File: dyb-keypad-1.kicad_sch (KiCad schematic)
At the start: 11 parts, among them J1 Conn_01x10, SW1 SW_Push_LED, SW2 SW_SPDT

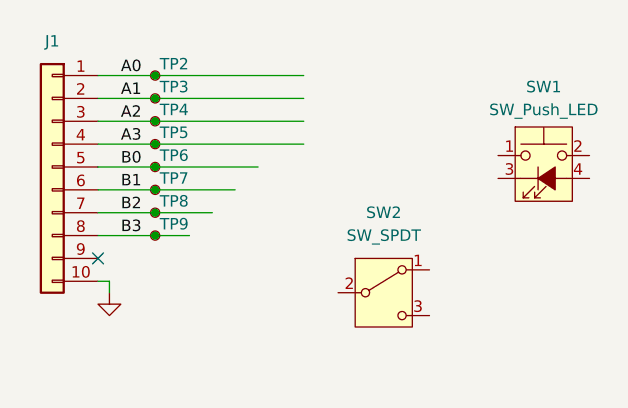
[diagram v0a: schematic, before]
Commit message: schem: fix output pin ordering
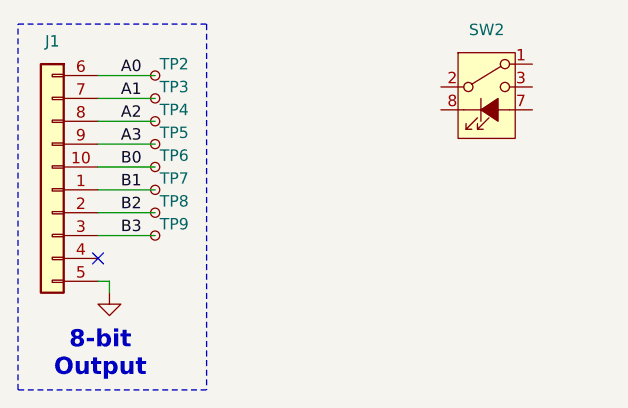
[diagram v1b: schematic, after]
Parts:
- removed SW1: SW_Push_LED, Button_Switch_THT:SW_NKK_GW12LJP, symbol Switch:SW_Push_LED
- removed SW2: SW_SPDT, Button_Switch_SMD:Nidec_Copal_CAS-120A, symbol Switch:SW_SPDT
- added SW2: SW_Push_LED_K6-6133D04, GLCS:SW_LED_K6-6133d04, symbol GLCS:SW_Push_LED_K6-6133D04
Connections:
- net A0: now also J1.6 (Pin_6); no longer J1.1 (Pin_1)
- net A1: now also J1.7 (Pin_7); no longer J1.2 (Pin_2)
- net A2: now also J1.8 (Pin_8); no longer J1.3 (Pin_3)
- net A3: now also J1.9 (Pin_9); no longer J1.4 (Pin_4)
- net B0: now also J1.10 (Pin_10); no longer J1.5 (Pin_5)
- net B1: now also J1.1 (Pin_1); no longer J1.6 (Pin_6)
- net B2: now also J1.2 (Pin_2); no longer J1.7 (Pin_7)
- net B3: now also J1.3 (Pin_3); no longer J1.8 (Pin_8)
- net GND: now also J1.5 (Pin_5); no longer J1.10 (Pin_10)
- new net: SW2.1, SW2.4
- new net: SW2.2, SW2.5
- new net: SW2.3, SW2.6
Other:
- note added: "8-bit Output"
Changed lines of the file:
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@@
 	(generator_version "10.0")
 	(paper "A4")
-	(junction
-		(at 58.42 62.23)
-		(diameter 0)
-		(color 0 0 0 0)
-	)
-	(junction
-		(at 58.42 44.45)
-		(diameter 0)
-		(color 0 0 0 0)
-	)
-	(junction
-		(at 58.42 46.99)
-		(diameter 0)
-		(color 0 0 0 0)
-	)
-	(junction
-		(at 58.42 59.69)
-		(diameter 0)
-		(color 0 0 0 0)
-	)
-	(junction
-		(at 58.42 57.15)
-		(diameter 0)
-		(color 0 0 0 0)
-	)
-	(junction
-		(at 58.42 52.07)
-		(diameter 0)
-		(color 0 0 0 0)
-	)
-	(junction
-		(at 58.42 54.61)
-		(diameter 0)
-		(color 0 0 0 0)
-	)
-	(junction
-		(at 58.42 49.53)
-		(diameter 0)
-		(color 0 0 0 0)
+	(rectangle
+		(start 43.18 38.735)
+		(end 64.135 79.375)
+		(stroke
+			(width 0)
+			(type dash)
+		)
+		(fill
+			(type none)
+		)
+	)
+	(text "8-bit\nOutput"
+		(exclude_from_sim no)
+		(at 52.324 75.438 0)
+		(effects
+			(font
+				(size 1.905 1.905)
+				(thickness 0.508)
+				(bold yes)
+			)
+		)
 	)
 	(no_connect
@@
 	(wire
 		(pts
-			(xy 58.42 62.23) (xy 62.23 62.23)
+			(xy 52.07 52.07) (xy 58.42 52.07)
 		)
 		(stroke
@@
 	(wire
 		(pts
-			(xy 52.07 52.07) (xy 58.42 52.07)
+			(xy 52.07 59.69) (xy 58.42 59.69)
 		)
 		(stroke
@@
 	(wire
 		(pts
-			(xy 52.07 59.69) (xy 58.42 59.69)
+			(xy 52.07 49.53) (xy 58.42 49.53)
 		)
 		(stroke
@@
 	(wire
 		(pts
-			(xy 52.07 49.53) (xy 58.42 49.53)
+			(xy 52.07 46.99) (xy 58.42 46.99)
 		)
 		(stroke
@@
 	(wire
 		(pts
-			(xy 58.42 59.69) (xy 64.77 59.69)
+			(xy 52.07 44.45) (xy 58.42 44.45)
 		)
 		(stroke
@@
 	(wire
 		(pts
-			(xy 52.07 46.99) (xy 58.42 46.99)
+			(xy 53.34 67.31) (xy 53.34 68.58)
 		)
 		(stroke
@@
 	(wire
 		(pts
-			(xy 58.42 57.15) (xy 67.31 57.15)
-		)
-		(stroke
-			(width 0)
-			(type default)
-		)
-	)
-	(wire
-		(pts
-			(xy 58.42 46.99) (xy 74.93 46.99)
-		)
-		(stroke
-			(width 0)
-			(type default)
-		)
-	)
-	(wire
-		(pts
-			(xy 52.07 44.45) (xy 58.42 44.45)
-		)
-		(stroke
-			(width 0)
-			(type default)
-		)
-	)
-	(wire
-		(pts
-			(xy 58.42 49.53) (xy 74.93 49.53)
-		)
-		(stroke
-			(width 0)
-			(type default)
-		)
-	)
-	(wire
-		(pts
-			(xy 53.34 67.31) (xy 53.34 68.58)
-		)
-		(stroke
-			(width 0)
-			(type default)
-		)
-	)
-	(wire
-		(pts
-			(xy 58.42 54.61) (xy 69.85 54.61)
-		)
-		(stroke
-			(width 0)
-			(type default)
-		)
-	)
-	(wire
-		(pts
 			(xy 52.07 57.15) (xy 58.42 57.15)
-		)
-		(stroke
-			(width 0)
-			(type default)
-		)
-	)
-	(wire
-		(pts
-			(xy 58.42 52.07) (xy 74.93 52.07)
-		)
-		(stroke
-			(width 0)
-			(type default)
-		)
-	)
-	(wire
-		(pts
-			(xy 58.42 44.45) (xy 74.93 44.45)
 		)
 		(stroke
@@
 	)
 	(symbol
-		(lib_id "Switch:SW_SPDT")
-		(at 83.82 68.58 0)
+		(lib_id "GLCS:SW_Push_LED_K6-6133D04")
+		(at 95.25 48.26 0)
 		(unit 1)
 		(body_style 1)
@@
 		(in_pos_files yes)
 		(dnp no)
-		(fields_autoplaced yes)
 		(property "Reference" "SW2"
-			(at 83.82 59.69 0)
-			(show_name no)
-			(do_not_autoplace no)
-			(effects
-				(font
-					(size 1.27 1.27)
-				)
-			)
-		)
-		(property "Value" "SW_SPDT"
-			(at 83.82 62.23 0)
-			(show_name no)
-			(do_not_autoplace no)
-			(effects
-				(font
-					(size 1.27 1.27)
-				)
-			)
-		)
-		(property "Footprint" "Button_Switch_SMD:Nidec_Copal_CAS-120A"
-			(at 83.82 68.58 0)
-			(hide yes)
-			(show_name no)
-			(do_not_autoplace no)
-			(effects
-				(font
-					(size 1.27 1.27)
-				)
-			)
-		)
-		(property "Datasheet" ""
-			(at 83.82 76.2 0)
-			(hide yes)
-			(show_name no)
-			(do_not_autoplace no)
-			(effects
-				(font
-					(size 1.27 1.27)
-				)
-			)
-		)
-		(property "Description" "Switch, single pole double throw"
-			(at 83.82 68.58 0)
-			(hide yes)
-			(show_name no)
-			(do_not_autoplace no)
-			(effects
-				(font
-					(size 1.27 1.27)
-				)
-			)
+			(at 95.25 39.37 0)
+			(show_name no)
+			(do_not_autoplace no)
+			(effects
+				(font
+					(size 1.27 1.27)
+				)
+			)
+		)
+		(property "Value" "SW_Push_LED_K6-6133D04"
+			(at 95.25 39.37 0)
+			(hide yes)
+			(show_name no)
+			(do_not_autoplace no)
+			(effects
+				(font
+					(size 1.27 1.27)
+				)
+			)
+		)
+		(property "Footprint" "GLCS:SW_LED_K6-6133d04"
+			(at 95.25 40.64 0)
+			(hide yes)
+			(show_name no)
+			(do_not_autoplace no)
+			(effects
+				(font
+					(size 1.27 1.27)
+				)
+			)
+		)
+		(property "Datasheet" "https://www.lcsc.com/datasheet/C128977.pdf"
+			(at 95.25 40.64 0)
+			(hide yes)
+			(show_name no)
+			(do_not_autoplace no)
+			(effects
+				(font
+					(size 1.27 1.27)
+				)
+			)
+		)
+		(property "Description" "Push button switch with LED, K6-6133D04-N1"
+			(at 95.25 48.26 0)
+			(hide yes)
+			(show_name no)
+			(do_not_autoplace no)
+			(effects
+				(font
+					(size 1.27 1.27)
+				)
+			)
+		)
+		(pin "1"
+		)
+		(pin "2"
+		)
+		(pin "4"
+		)
+		(pin "7"
+		)
+		(pin "8"
 		)
 		(pin "3"
 		)
-		(pin "2"
-		)
-		(pin "1"
+		(pin "6"
+		)
+		(pin "5"
 		)
 		(instances
@@
 					(unit 1)
 				)
-			)
-		)
-	)
-	(symbol
-		(lib_id "Switch:SW_Push_LED")
-		(at 101.6 55.88 0)
-		(unit 1)
-		(body_style 1)
-		(exclude_from_sim no)
-		(in_bom yes)
-		(on_board yes)
-		(in_pos_files yes)
-		(dnp no)
-		(fields_autoplaced yes)
-		(property "Reference" "SW1"
-			(at 101.6 45.72 0)
-			(show_name no)
-			(do_not_autoplace no)
-			(effects
-				(font
-					(size 1.27 1.27)
-				)
-			)
-		)
-		(property "Value" "SW_Push_LED"
-			(at 101.6 48.26 0)
-			(show_name no)
-			(do_not_autoplace no)
-			(effects
-				(font
-					(size 1.27 1.27)
-				)
-			)
-		)
-		(property "Footprint" "Button_Switch_THT:SW_NKK_GW12LJP"
-			(at 101.6 48.26 0)
-			(hide yes)
-			(show_name no)
-			(do_not_autoplace no)
-			(effects
-				(font
-					(size 1.27 1.27)
-				)
-			)
-		)
-		(property "Datasheet" ""
-			(at 101.6 48.26 0)
-			(hide yes)
-			(show_name no)
-			(do_not_autoplace no)
-			(effects
-				(font
-					(size 1.27 1.27)
-				)
-			)
-		)
-		(property "Description" "Push button switch with LED, generic"
-			(at 101.6 55.88 0)
-			(hide yes)
-			(show_name no)
-			(do_not_autoplace no)
-			(effects
-				(font
-					(size 1.27 1.27)
-				)
-			)
-		)
-		(pin "2"
-		)
-		(pin "1"
-		)
-		(pin "3"
-		)
-		(pin "4"
-		)
-		(instances
-			(project "dyb-keypad-1"
-				(path "/8a92ff1d-0247-4ed8-a25c-ec6e0e8e6922"
-					(reference "SW1")
-					(unit 1)
-				)
